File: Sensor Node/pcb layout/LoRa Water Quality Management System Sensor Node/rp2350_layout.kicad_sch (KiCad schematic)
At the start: 28 parts, among them J8 Conn_01x02, J9 Conn_01x03, U7 W25Q128JVSIQ TR, U8 RP2350_60QFN, Y1 ABM8-272-T3

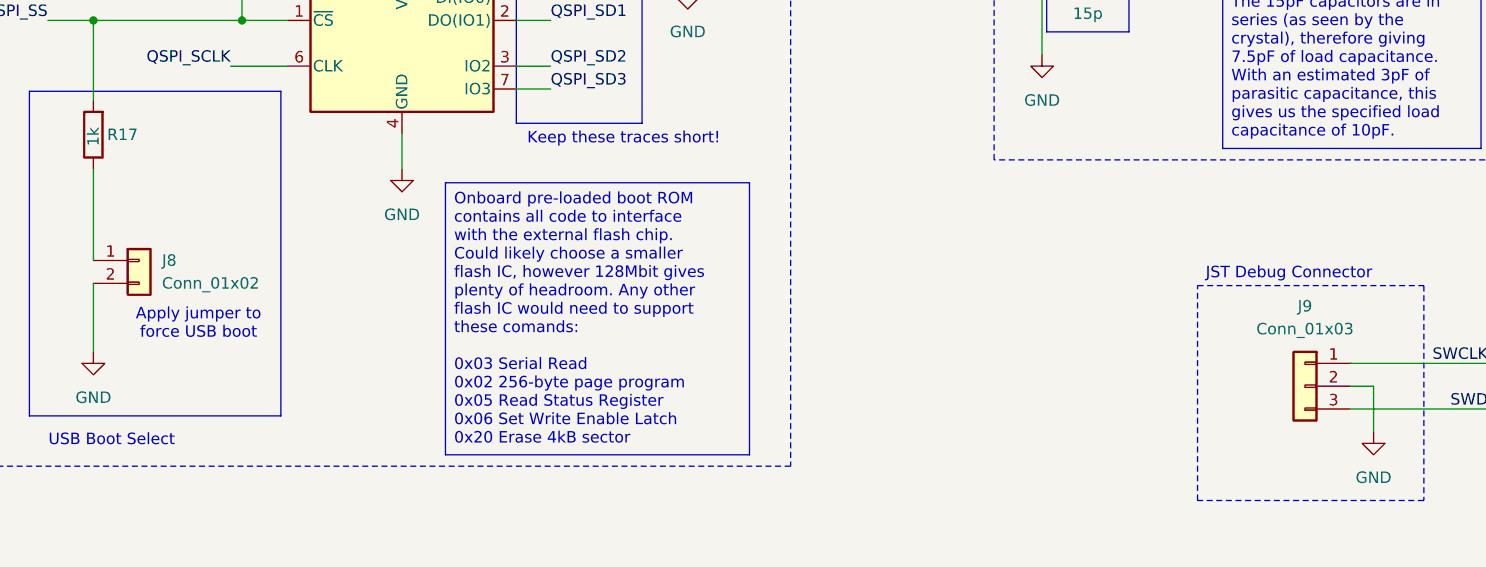
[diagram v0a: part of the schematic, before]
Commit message: Improve RF routing and noise immunity. Add copper pours on top and bottom layer with ample stitching vias. Add TVS diodes for ESD protection and testpoints for hardware debugging.
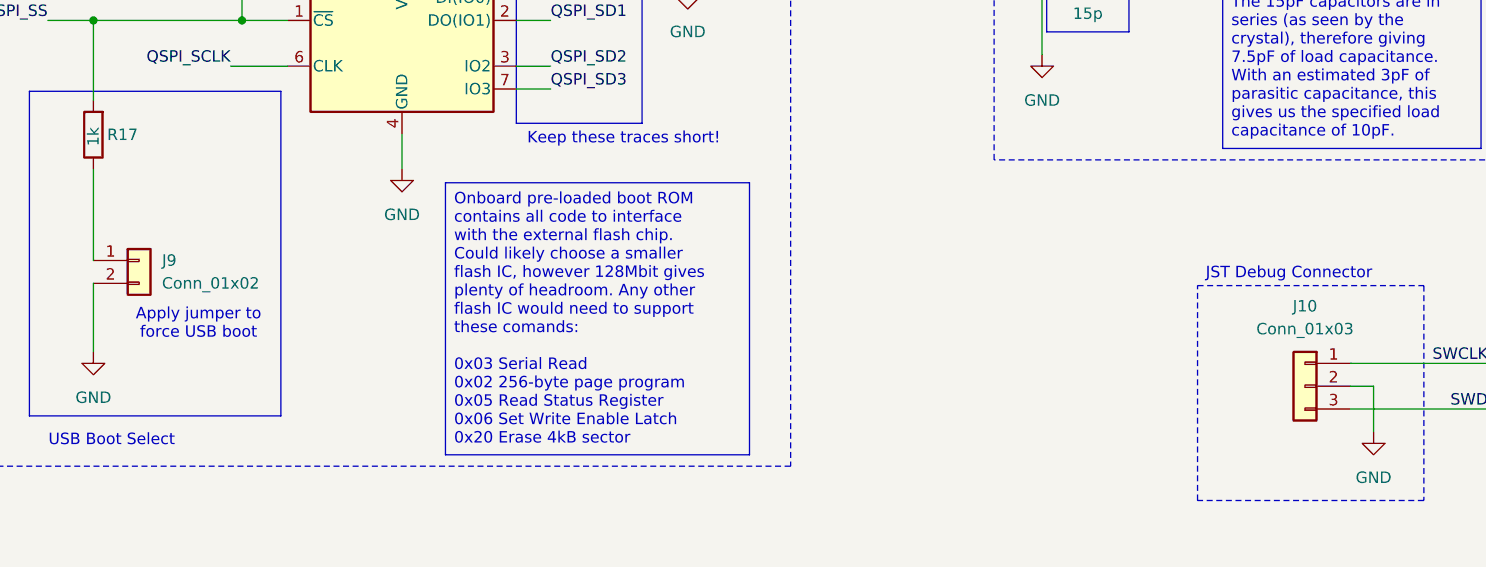
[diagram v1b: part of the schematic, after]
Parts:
- renumbered J9 to J10, J8 to J9
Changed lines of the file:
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@@
 		(dnp no)
 		(fields_autoplaced yes)
-		(property "Reference" "#PWR047"
+		(property "Reference" "#PWR050"
 			(at 190.5 223.52 0)
 			(effects
@@
 			(project ""
 				(path "/f090528b-8c52-4bf9-a2b8-0c17aa5e5727/8ed505b3-7460-4c84-b5db-8c51c81aa9b0"
-					(reference "#PWR047")
+					(reference "#PWR050")
 					(unit 1)
 				)
@@
 		(dnp no)
 		(fields_autoplaced yes)
-		(property "Reference" "#PWR045"
+		(property "Reference" "#PWR048"
 			(at 179.07 162.56 0)
 			(effects
@@
 			(project ""
 				(path "/f090528b-8c52-4bf9-a2b8-0c17aa5e5727/8ed505b3-7460-4c84-b5db-8c51c81aa9b0"
-					(reference "#PWR045")
+					(reference "#PWR048")
 					(unit 1)
 				)
@@
 		(dnp no)
 		(fields_autoplaced yes)
-		(property "Reference" "J8"
+		(property "Reference" "J9"
 			(at 55.88 198.1199 0)
 			(effects
@@
 			(project ""
 				(path "/f090528b-8c52-4bf9-a2b8-0c17aa5e5727/8ed505b3-7460-4c84-b5db-8c51c81aa9b0"
-					(reference "J8")
+					(reference "J9")
 					(unit 1)
 				)
@@
 		(dnp no)
 		(fields_autoplaced yes)
-		(property "Reference" "#PWR048"
+		(property "Reference" "#PWR051"
 			(at 208.28 66.04 0)
 			(effects
@@
 			(project ""
 				(path "/f090528b-8c52-4bf9-a2b8-0c17aa5e5727/8ed505b3-7460-4c84-b5db-8c51c81aa9b0"
-					(reference "#PWR048")
+					(reference "#PWR051")
 					(unit 1)
 				)
@@
 		(dnp no)
 		(fields_autoplaced yes)
-		(property "Reference" "#PWR039"
+		(property "Reference" "#PWR042"
 			(at 82.55 194.31 0)
 			(effects
@@
 			(project "LoRa Water Quality Management System Sensor Node"
 				(path "/f090528b-8c52-4bf9-a2b8-0c17aa5e5727/8ed505b3-7460-4c84-b5db-8c51c81aa9b0"
-					(reference "#PWR039")
+					(reference "#PWR042")
 					(unit 1)
 				)
@@
 		(dnp no)
 		(fields_autoplaced yes)
-		(property "Reference" "#PWR049"
+		(property "Reference" "#PWR052"
 			(at 210.82 111.76 0)
 			(effects
@@
 			(project ""
 				(path "/f090528b-8c52-4bf9-a2b8-0c17aa5e5727/8ed505b3-7460-4c84-b5db-8c51c81aa9b0"
-					(reference "#PWR049")
+					(reference "#PWR052")
 					(unit 1)
 				)
@@
 		(dnp no)
 		(fields_autoplaced yes)
-		(property "Reference" "#PWR053"
+		(property "Reference" "#PWR056"
 			(at 375.92 90.17 0)
 			(effects
@@
 			(project ""
 				(path "/f090528b-8c52-4bf9-a2b8-0c17aa5e5727/8ed505b3-7460-4c84-b5db-8c51c81aa9b0"
-					(reference "#PWR053")
+					(reference "#PWR056")
 					(unit 1)
 				)
@@
 		(dnp no)
 		(fields_autoplaced yes)
-		(property "Reference" "#PWR050"
+		(property "Reference" "#PWR053"
 			(at 245.11 44.45 0)
 			(effects
@@
 			(project "LoRa Water Quality Management System Sensor Node"
 				(path "/f090528b-8c52-4bf9-a2b8-0c17aa5e5727/8ed505b3-7460-4c84-b5db-8c51c81aa9b0"
-					(reference "#PWR050")
+					(reference "#PWR053")
 					(unit 1)
 				)
@@
 		(on_board yes)
 		(dnp no)
-		(property "Reference" "#PWR044"
+		(property "Reference" "#PWR047"
 			(at 170.18 128.27 0)
 			(effects
@@
 			(project ""
 				(path "/f090528b-8c52-4bf9-a2b8-0c17aa5e5727/8ed505b3-7460-4c84-b5db-8c51c81aa9b0"
-					(reference "#PWR044")
+					(reference "#PWR047")
 					(unit 1)
 				)
@@
 		(dnp no)
 		(fields_autoplaced yes)
-		(property "Reference" "#PWR042"
+		(property "Reference" "#PWR045"
 			(at 166.37 162.56 0)
 			(effects
@@
 			(project "LoRa Water Quality Management System Sensor Node"
 				(path "/f090528b-8c52-4bf9-a2b8-0c17aa5e5727/8ed505b3-7460-4c84-b5db-8c51c81aa9b0"
-					(reference "#PWR042")
+					(reference "#PWR045")
 					(unit 1)
 				)
@@
 		(dnp no)
 		(fields_autoplaced yes)
-		(property "Reference" "#PWR037"
+		(property "Reference" "#PWR040"
 			(at 48.26 214.63 0)
 			(effects
@@
 			(project ""
 				(path "/f090528b-8c52-4bf9-a2b8-0c17aa5e5727/8ed505b3-7460-4c84-b5db-8c51c81aa9b0"
-					(reference "#PWR037")
+					(reference "#PWR040")
 					(unit 1)
 				)
@@
 		(dnp no)
 		(fields_autoplaced yes)
-		(property "Reference" "#PWR038"
+		(property "Reference" "#PWR041"
 			(at 82.55 153.67 0)
 			(effects
@@
 			(project ""
 				(path "/f090528b-8c52-4bf9-a2b8-0c17aa5e5727/8ed505b3-7460-4c84-b5db-8c51c81aa9b0"
-					(reference "#PWR038")
+					(reference "#PWR041")
 					(unit 1)
 				)
@@
 		(dnp no)
 		(fields_autoplaced yes)
-		(property "Reference" "#PWR040"
+		(property "Reference" "#PWR043"
 			(at 114.3 173.99 0)
 			(effects
@@
 			(project "LoRa Water Quality Management System Sensor Node"
 				(path "/f090528b-8c52-4bf9-a2b8-0c17aa5e5727/8ed505b3-7460-4c84-b5db-8c51c81aa9b0"
-					(reference "#PWR040")
+					(reference "#PWR043")
 					(unit 1)
 				)
@@
 		(dnp no)
 		(fields_autoplaced yes)
-		(property "Reference" "#PWR052"
+		(property "Reference" "#PWR055"
 			(at 284.48 53.34 0)
 			(effects
@@
 			(project ""
 				(path "/f090528b-8c52-4bf9-a2b8-0c17aa5e5727/8ed505b3-7460-4c84-b5db-8c51c81aa9b0"
-					(reference "#PWR052")
+					(reference "#PWR055")
 					(unit 1)
 				)
@@
 		(dnp no)
 		(fields_autoplaced yes)
-		(property "Reference" "#PWR051"
+		(property "Reference" "#PWR054"
 			(at 267.97 213.36 0)
 			(effects
@@
 			(project ""
 				(path "/f090528b-8c52-4bf9-a2b8-0c17aa5e5727/8ed505b3-7460-4c84-b5db-8c51c81aa9b0"
-					(reference "#PWR051")
+					(reference "#PWR054")
 					(unit 1)
 				)
@@
 		(dnp no)
 		(fields_autoplaced yes)
-		(property "Reference" "J9"
+		(property "Reference" "J10"
 			(at 182.88 203.2 0)
 			(effects
@@
 			(project ""
 				(path "/f090528b-8c52-4bf9-a2b8-0c17aa5e5727/8ed505b3-7460-4c84-b5db-8c51c81aa9b0"
-					(reference "J9")
+					(reference "J10")
 					(unit 1)
 				)
@@
 		(dnp no)
 		(fields_autoplaced yes)
-		(property "Reference" "#PWR046"
+		(property "Reference" "#PWR049"
 			(at 181.61 106.68 0)
 			(effects
@@
 			(project ""
 				(path "/f090528b-8c52-4bf9-a2b8-0c17aa5e5727/8ed505b3-7460-4c84-b5db-8c51c81aa9b0"
-					(reference "#PWR046")
+					(reference "#PWR049")
 					(unit 1)
 				)
@@
 		(dnp no)
 		(fields_autoplaced yes)
-		(property "Reference" "#PWR043"
+		(property "Reference" "#PWR046"
 			(at 170.18 90.17 0)
 			(effects
@@
 			(project ""
 				(path "/f090528b-8c52-4bf9-a2b8-0c17aa5e5727/8ed505b3-7460-4c84-b5db-8c51c81aa9b0"
-					(reference "#PWR043")
+					(reference "#PWR046")
 					(unit 1)
 				)
@@
 		(dnp no)
 		(fields_autoplaced yes)
-		(property "Reference" "#PWR041"
+		(property "Reference" "#PWR044"
 			(at 153.67 181.61 0)
 			(effects
@@
 			(project "LoRa Water Quality Management System Sensor Node"
 				(path "/f090528b-8c52-4bf9-a2b8-0c17aa5e5727/8ed505b3-7460-4c84-b5db-8c51c81aa9b0"
-					(reference "#PWR041")
-					(unit 1)
-				)
+					(reference "#PWR044")
+					(unit 1)
+				)
